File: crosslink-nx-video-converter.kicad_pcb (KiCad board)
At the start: 2 copper layers, 0 parts

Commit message: Added DDR3 Vtt and Vref regulator
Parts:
- added C1: C_1u_0603, antmicro-footprints:0603-cap, F.Cu at (128.0, 96.0)
- added C10: C_100n_0603, antmicro-footprints:0603-cap, F.Cu at (142.8, 79.0)
- added C11: C_100n_0603, antmicro-footprints:0603-cap, F.Cu at (131.6, 90.2)
- added C12: C_100n_0603, antmicro-footprints:0603-cap, F.Cu at (135.7, 79.4)
- added C13: C_22u_0805, antmicro-footprints:0805-cap, F.Cu at (126.8, 88.4)
- added C14: C_22u_0805, antmicro-footprints:0805-cap, F.Cu at (138.2, 76.7)
- added C15: C_22u_0805, antmicro-footprints:0805-cap, F.Cu at (131.5, 82.5)
- added C16: C_22u_0805, antmicro-footprints:0805-cap, F.Cu at (126.7, 82.5)
- added C17: C_22u_0805, antmicro-footprints:0805-cap, F.Cu at (126.7, 79.6)
- added C18: C_22u_0805, antmicro-footprints:0805-cap, F.Cu at (131.5, 79.6)
- added C19: C_22u_0805, antmicro-footprints:0805-cap, F.Cu at (138.2, 73.8)
- added C2: C_1u_0603, antmicro-footprints:0603-cap, F.Cu at (131.0, 85.2)
- added C20: C_22u_0805, antmicro-footprints:0805-cap, F.Cu at (133.3, 76.7)
- added C21: C_22u_0805, antmicro-footprints:0805-cap, F.Cu at (143.1, 73.8)
- added C22: C_22u_0805, antmicro-footprints:0805-cap, F.Cu at (128.5, 76.7)
- added C23: C_22u_0805, antmicro-footprints:0805-cap, F.Cu at (115.4, 94.1)
- added C24: C_22u_0805, antmicro-footprints:0805-cap, F.Cu at (133.3, 73.8)
- added C25: C_100n_0402, antmicro-footprints:0402-cap, F.Cu at (146.1, 95.6)
- added C26: C_100n_0402, antmicro-footprints:0402-cap, F.Cu at (144.5, 93.6)
- added C27: C_100n_0402, antmicro-footprints:0402-cap, F.Cu at (139.0, 101.0)
- added C28: C_100n_0402, antmicro-footprints:0402-cap, F.Cu at (139.0, 103.0)
- added C29: C_100n_0402, antmicro-footprints:0402-cap, F.Cu at (140.3, 99.0)
- added C3: C_1u_0603, antmicro-footprints:0603-cap, F.Cu at (150.8, 73.6)
- added C30: C_100n_0402, antmicro-footprints:0402-cap, F.Cu at (136.1, 102.3)
- added C31: C_100n_0402, antmicro-footprints:0402-cap, F.Cu at (147.4, 93.6)
- added C32: C_100n_0402, antmicro-footprints:0402-cap, F.Cu at (136.1, 104.3)
- added C33: C_100n_0402, antmicro-footprints:0402-cap, F.Cu at (143.2, 97.0)
- added C34: C_100n_0402, antmicro-footprints:0402-cap, F.Cu at (143.2, 99.0)
- added C4: C_1u_0603, antmicro-footprints:0603-cap, F.Cu at (131.0, 87.7)
- added C5: C_1u_0603, antmicro-footprints:0603-cap, F.Cu at (145.9, 76.5)
- added C6: C_1u_0603, antmicro-footprints:0603-cap, F.Cu at (149.5, 76.1)
- added C7: C_10u_0603, antmicro-footprints:0603-cap, F.Cu at (135.7, 84.4)
- added C8: C_10u_0603, antmicro-footprints:0603-cap, F.Cu at (124.5, 96.0)
- added C9: C_10u_0603, antmicro-footprints:0603-cap, F.Cu at (138.1, 86.8)
- added L1: DJNR5020-3R3-S, crosslink-nx-video-converter:L_4.9x4.9mm, F.Cu at (118.1, 75.9)
- added L2: DJNR5020-3R3-S, crosslink-nx-video-converter:L_4.9x4.9mm, F.Cu at (111.5, 75.9)
- added L3: DJNR5020-3R3-S, crosslink-nx-video-converter:L_4.9x4.9mm, F.Cu at (111.5, 82.9)
- added R1: R_0R_0603, antmicro-footprints:0603-res, F.Cu at (128.0, 93.5)
- added R10: R_0R_0603, antmicro-footprints:0603-res, F.Cu at (142.8, 81.5)
- added R11: R_0R_0603, antmicro-footprints:0603-res, F.Cu at (134.6, 86.8)
- added R12: R_0R_0603, antmicro-footprints:0603-res, F.Cu at (135.7, 81.9)
- added R13: R_0R_0805, antmicro-footprints:0805-res, F.Cu at (126.8, 85.5)
- added R14: R_0R_0805, antmicro-footprints:0805-res, F.Cu at (115.4, 91.2)
- added R15: R_0R_0805, antmicro-footprints:0805-res, F.Cu at (128.5, 73.8)
- added R16: R_33k_0603, antmicro-footprints:0603-res, F.Cu at (139.2, 81.9)
- added R17: R_10k_0603, antmicro-footprints:0603-res, F.Cu at (131.6, 95.1)
- added R18: R_3k01_1%_0603, antmicro-footprints:0603-res, F.Cu at (142.8, 83.9)
- added R19: R_10k_1%_0603, antmicro-footprints:0603-res, F.Cu at (139.2, 84.4)
- added R2: R_0R_0603, antmicro-footprints:0603-res, F.Cu at (142.4, 76.5)
- added R20: R_13k7_1%_0603, antmicro-footprints:0603-res, F.Cu at (146.3, 81.5)
- added R21: R_20k_1%_0603, antmicro-footprints:0603-res, F.Cu at (147.2, 73.6)
- added R22: R_0R_0805, antmicro-footprints:0805-res, F.Cu at (122.0, 85.9)
- added R23: R_0R_0805, antmicro-footprints:0805-res, F.Cu at (120.2, 91.2)
- added R24: R_0R_0805, antmicro-footprints:0805-res, F.Cu at (120.2, 94.1)
- added R25: R_100R_0402, antmicro-footprints:0402-res, F.Cu at (148.7, 90.2)
- added R26: 4x51R_0402_array, antmicro-footprints:R_Array_4x0402, F.Cu at (140.9, 93.9)
- added R27: 4x51R_0402_array, antmicro-footprints:R_Array_4x0402, F.Cu at (145.2, 90.5)
- added R28: 4x51R_0402_array, antmicro-footprints:R_Array_4x0402, F.Cu at (135.8, 97.3)
- added R29: 4x51R_0402_array, antmicro-footprints:R_Array_4x0402, F.Cu at (167.2, 85.6)
- added R3: R_0R_0603, antmicro-footprints:0603-res, F.Cu at (131.6, 92.7)
- added R30: 4x51R_0402_array, antmicro-footprints:R_Array_4x0402, F.Cu at (140.9, 90.5)
- added R31: 4x51R_0402_array, antmicro-footprints:R_Array_4x0402, F.Cu at (136.8, 90.5)
- added R32: R_240R_1%_0402, antmicro-footprints:0402-res, F.Cu at (140.3, 97.0)
- added R33: R_1k_0402, antmicro-footprints:0402-res, F.Cu at (136.1, 100.4)
- added R34: R_1k_0402, antmicro-footprints:0402-res, F.Cu at (151.6, 90.2)
- added R4: R_3k01_1%_0603, antmicro-footprints:0603-res, F.Cu at (146.3, 79.0)
- added R5: R_10k_1%_0603, antmicro-footprints:0603-res, F.Cu at (128.0, 91.1)
- added R6: R_12k_0603, antmicro-footprints:0603-res, F.Cu at (124.5, 93.5)
- added R7: R_24k_0603, antmicro-footprints:0603-res, F.Cu at (139.2, 79.4)
- added R8: R_18k7_1%_0603, antmicro-footprints:0603-res, F.Cu at (135.1, 89.3)
- added R9: R_15k_0603, antmicro-footprints:0603-res, F.Cu at (124.5, 91.1)
- added TP1: TP, antmicro-footprints:TP-R-1.5, F.Cu at (141.7, 101.2)
- added U1: AP7330-W5-7, antmicro-footprints:SOT-23-5, F.Cu at (123.7, 75.0)
- added U2: AP7330-W5-7, antmicro-footprints:SOT-23-5, F.Cu at (110.6, 89.1)
- added U3: AP7330-W5-7, antmicro-footprints:SOT-23-5, F.Cu at (117.2, 82.0)
- added U4: AP62301WU-7, antmicro-footprints:TSOT23-6, F.Cu at (121.9, 81.9)
- added U5: AP62301WU-7, antmicro-footprints:TSOT23-6, F.Cu at (110.6, 94.2)
- added U6: AP62301WU-7, antmicro-footprints:TSOT23-6, F.Cu at (117.2, 87.2)
- added U7: MT41K128M16JT-125_K, antmicro-footprints:BGA80P96C6X16_800X1400X110, F.Cu at (161.6, 80.2)

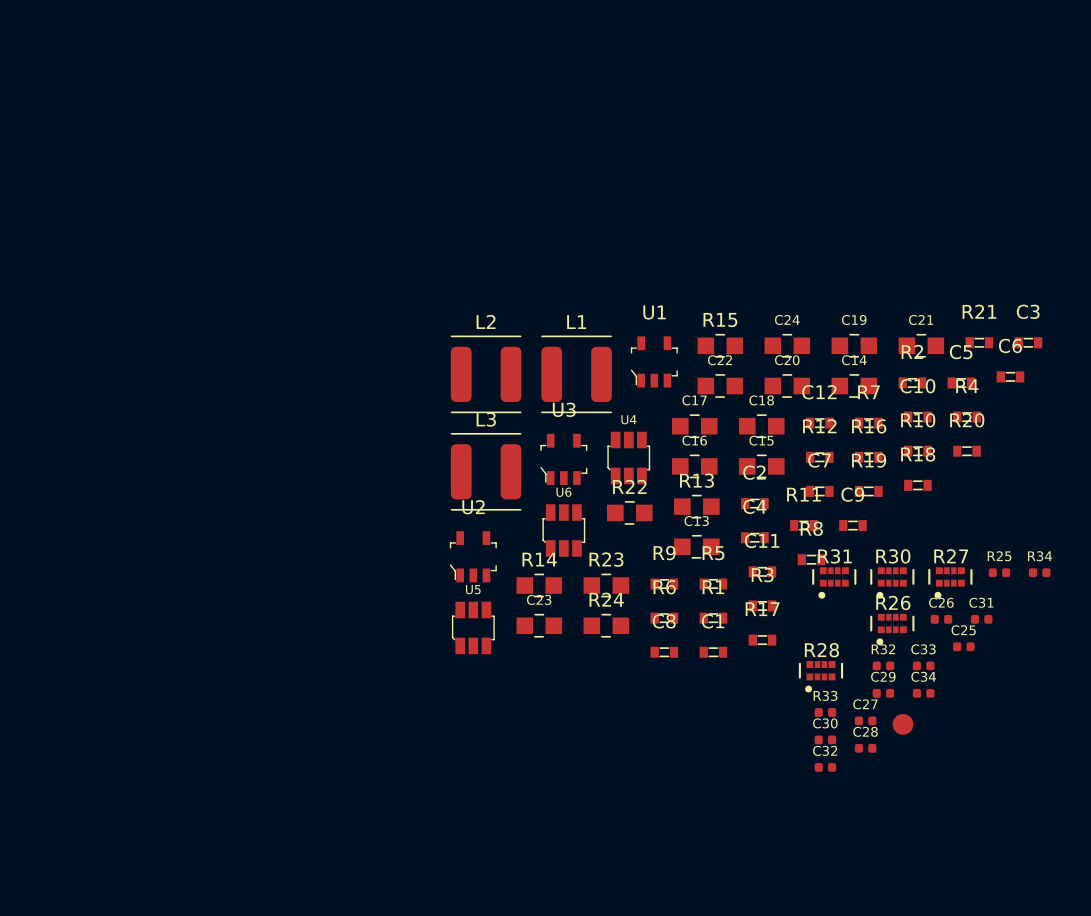
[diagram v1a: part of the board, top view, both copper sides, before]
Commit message: Connected FPGA to power supply and added power filtering
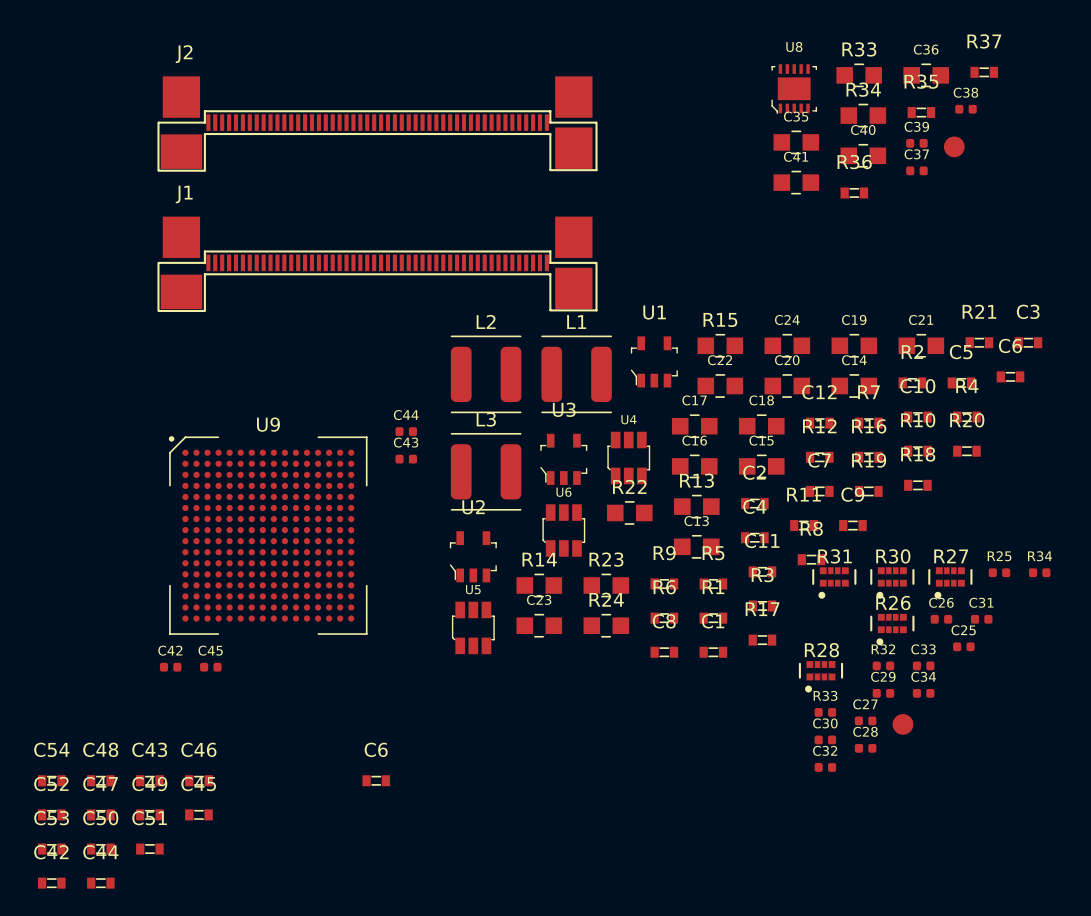
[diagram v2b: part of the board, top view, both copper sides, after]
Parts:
- added C35: C_22u_0805, antmicro-footprints:0805-cap, F.Cu at (134.0, 59.1)
- added C36: C_22u_0805, antmicro-footprints:0805-cap, F.Cu at (143.4, 54.2)
- added C37: C_100n_0402, antmicro-footprints:0402-cap, F.Cu at (142.7, 61.2)
- added C38: C_100n_0402, antmicro-footprints:0402-cap, F.Cu at (146.3, 56.7)
- added C39: C_100n_0402, antmicro-footprints:0402-cap, F.Cu at (142.7, 59.2)
- added C40: C_22u_0805, antmicro-footprints:0805-cap, F.Cu at (138.8, 60.1)
- added C41: C_22u_0805, antmicro-footprints:0805-cap, F.Cu at (134.0, 62.0)
- added C42: C_100n_0402, antmicro-footprints:0402-cap, F.Cu at (88.7, 97.1)
- added C42: C_100n_0603, antmicro-footprints:0603-cap, F.Cu at (80.1, 112.7)
- added C43: C_100n_0603, antmicro-footprints:0603-cap, F.Cu at (87.2, 105.3)
- added C43: C_100n_0402, antmicro-footprints:0402-cap, F.Cu at (105.8, 82.0)
- added C44: C_100n_0603, antmicro-footprints:0603-cap, F.Cu at (83.7, 112.7)
- added C44: C_100n_0402, antmicro-footprints:0402-cap, F.Cu at (105.8, 80.0)
- added C45: C_100n_0603, antmicro-footprints:0603-cap, F.Cu at (90.8, 107.8)
- added C45: C_100n_0402, antmicro-footprints:0402-cap, F.Cu at (91.6, 97.1)
- added C46: C_100n_0603, antmicro-footprints:0603-cap, F.Cu at (90.8, 105.3)
- added C47: C_100n_0603, antmicro-footprints:0603-cap, F.Cu at (83.7, 107.8)
- added C48: C_100n_0603, antmicro-footprints:0603-cap, F.Cu at (83.7, 105.3)
- added C49: C_100n_0603, antmicro-footprints:0603-cap, F.Cu at (87.2, 107.8)
- added C50: C_100n_0603, antmicro-footprints:0603-cap, F.Cu at (83.7, 110.2)
- added C51: C_100n_0603, antmicro-footprints:0603-cap, F.Cu at (87.2, 110.2)
- added C52: C_100n_0603, antmicro-footprints:0603-cap, F.Cu at (80.1, 107.8)
- added C53: C_100n_0603, antmicro-footprints:0603-cap, F.Cu at (80.1, 110.2)
- added C54: C_100n_0603, antmicro-footprints:0603-cap, F.Cu at (80.1, 105.3)
- added C6: C_10u_0603, antmicro-footprints:0603-cap, F.Cu at (103.6, 105.3)
- added J1: WE_68715014522, antmicro-footprints:WE_68715014522, F.Cu at (103.7, 67.2)
- added J2: WE_68715014522, antmicro-footprints:WE_68715014522, F.Cu at (103.7, 57.1)
- added R33: R_0R_0805, antmicro-footprints:0805-res, F.Cu at (138.6, 54.2)
- added R34: R_0R_0805, antmicro-footprints:0805-res, F.Cu at (138.8, 57.2)
- added R35: R_10k_1%_0603, antmicro-footprints:0603-res, F.Cu at (143.1, 56.9)
- added R36: R_10k_1%_0603, antmicro-footprints:0603-res, F.Cu at (138.2, 62.8)
- added R37: R_100k_0603, antmicro-footprints:0603-res, F.Cu at (147.6, 54.0)
- added TP2: TP, antmicro-footprints:TP-R-1.5, F.Cu at (145.4, 59.4)
- added U8: NCV51200MNTXG, antmicro-footprints:DFN-10-1EP_3x3mm, F.Cu at (133.8, 55.2)
- added U9: LIFCL-40-9BG256C, antmicro-footprints:BGA-256_16x16_14.0x14.0mm, F.Cu at (95.8, 87.6)
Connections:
- net /DDR3/DDR3_A0 renamed DDR3_A0
- net /DDR3/DDR3_A1 renamed DDR3_A1
- net /DDR3/DDR3_A10 renamed DDR3_A10
- net /DDR3/DDR3_A11 renamed DDR3_A11
- net /DDR3/DDR3_A12 renamed DDR3_A12
- net /DDR3/DDR3_A13 renamed DDR3_A13
- net /DDR3/DDR3_A2 renamed DDR3_A2
- net /DDR3/DDR3_A3 renamed DDR3_A3
- net /DDR3/DDR3_A4 renamed DDR3_A4
- net /DDR3/DDR3_A5 renamed DDR3_A5
- net /DDR3/DDR3_A6 renamed DDR3_A6
- net /DDR3/DDR3_A7 renamed DDR3_A7
- net /DDR3/DDR3_A8 renamed DDR3_A8
- net /DDR3/DDR3_A9 renamed DDR3_A9
- net /DDR3/DDR3_BA0 renamed DDR3_BA0
- net /DDR3/DDR3_BA1 renamed DDR3_BA1
- net /DDR3/DDR3_BA2 renamed DDR3_BA2
- net /DDR3/DDR3_CKE renamed DDR3_CKE
- net /DDR3/DDR3_CK_N renamed DDR3_CK_N
- net /DDR3/DDR3_CK_P renamed DDR3_CK_P
- net /DDR3/DDR3_ODT renamed DDR3_ODT
- net /DDR3/~{DDR3_CAS} renamed ~{DDR3_CAS}
- net /DDR3/~{DDR3_CS} renamed ~{DDR3_CS}
- net /DDR3/~{DDR3_RAS} renamed ~{DDR3_RAS}
- net /DDR3/~{DDR3_RESET} renamed ~{DDR3_RESET}
- net /DDR3/~{DDR3_WE} renamed ~{DDR3_WE}
- C33 pad 2: Net-(C33-Pad2) -> Vref
- C34 pad 1: Net-(C33-Pad2) -> Vref
- U7 pad A2: /DDR3/DDR3_DQ13 -> DDR3_DQ13
- U7 pad A3: /DDR3/DDR3_DQ15 -> DDR3_DQ15
- U7 pad A7: /DDR3/DDR3_DQ12 -> DDR3_DQ12
- U7 pad B7: /DDR3/DDR3_UDQS_N -> DDR3_UDQS_N
- U7 pad B8: /DDR3/DDR3_DQ14 -> DDR3_DQ14
- U7 pad C2: /DDR3/DDR3_DQ11 -> DDR3_DQ11
- U7 pad C3: /DDR3/DDR3_DQ9 -> DDR3_DQ9
- U7 pad C7: /DDR3/DDR3_UDQS_P -> DDR3_UDQS_P
- U7 pad C8: /DDR3/DDR3_DQ10 -> DDR3_DQ10
- U7 pad D3: /DDR3/DDR3_UDM -> DDR3_UDM
- U7 pad D7: /DDR3/DDR3_DQ8 -> DDR3_DQ8
- U7 pad E3: /DDR3/DDR3_DQ0 -> DDR3_DQ0
- U7 pad E7: /DDR3/DDR3_LDM -> DDR3_LDM
- U7 pad F2: /DDR3/DDR3_DQ2 -> DDR3_DQ2
- U7 pad F3: /DDR3/DDR3_LDQS_P -> DDR3_LDQS_P
- U7 pad F7: /DDR3/DDR3_DQ1 -> DDR3_DQ1
- U7 pad F8: /DDR3/DDR3_DQ3 -> DDR3_DQ3
- U7 pad G2: /DDR3/DDR3_DQ6 -> DDR3_DQ6
- U7 pad G3: /DDR3/DDR3_LDQS_N -> DDR3_LDQS_N
- U7 pad H1: Net-(C33-Pad2) -> Vref
- U7 pad H3: /DDR3/DDR3_DQ4 -> DDR3_DQ4
- U7 pad H7: /DDR3/DDR3_DQ7 -> DDR3_DQ7
- U7 pad H8: /DDR3/DDR3_DQ5 -> DDR3_DQ5
- U7 pad M8: Net-(C33-Pad2) -> Vref
